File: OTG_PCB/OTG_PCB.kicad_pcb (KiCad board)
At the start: 2 copper layers, 44.9 x 35 mm, 14 parts, among them J1 USB_C_Receptacle_USB2.0, J2 USB_MINI_B, J3 USB_A, J4 USB_MINI_B, J5 USB_C_Receptacle_USB2.0, U1 USB3740B-AI2, U2 TUSB320IRWBR

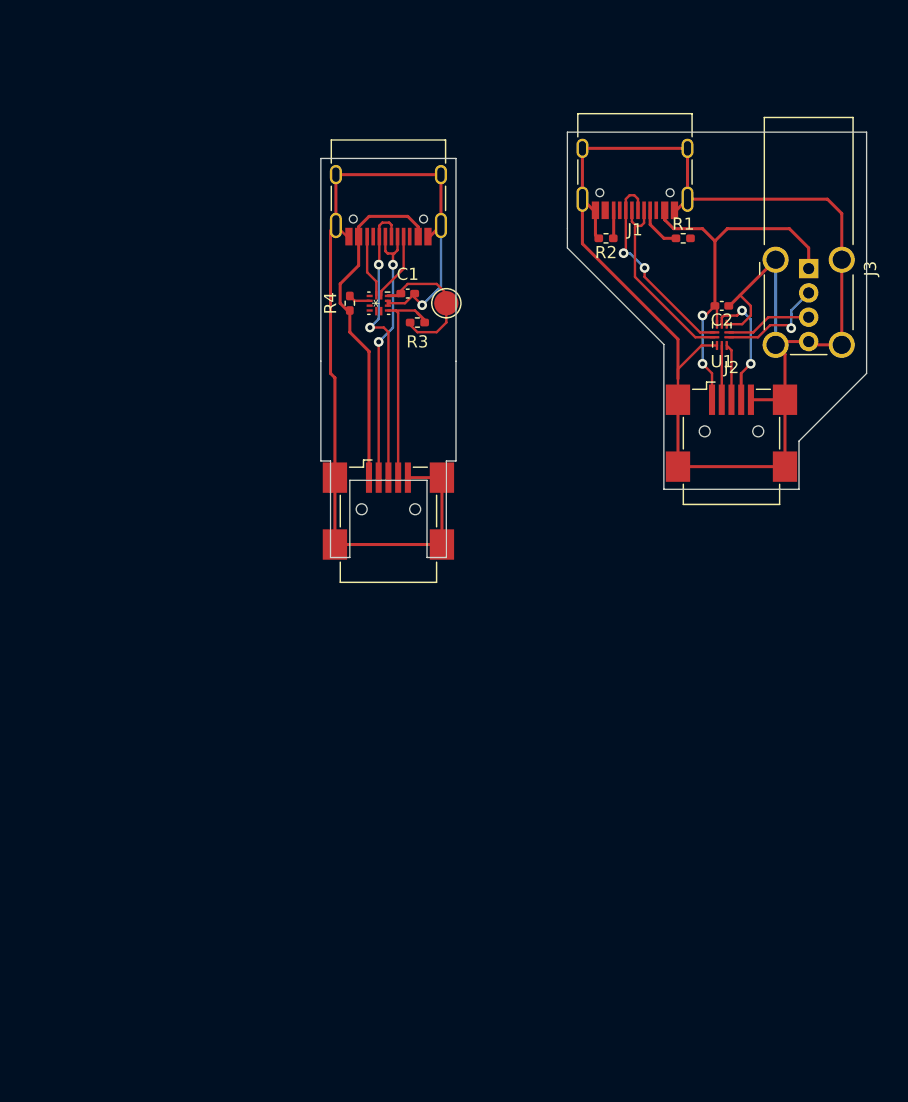
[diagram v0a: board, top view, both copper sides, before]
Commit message: Single layer, flex only
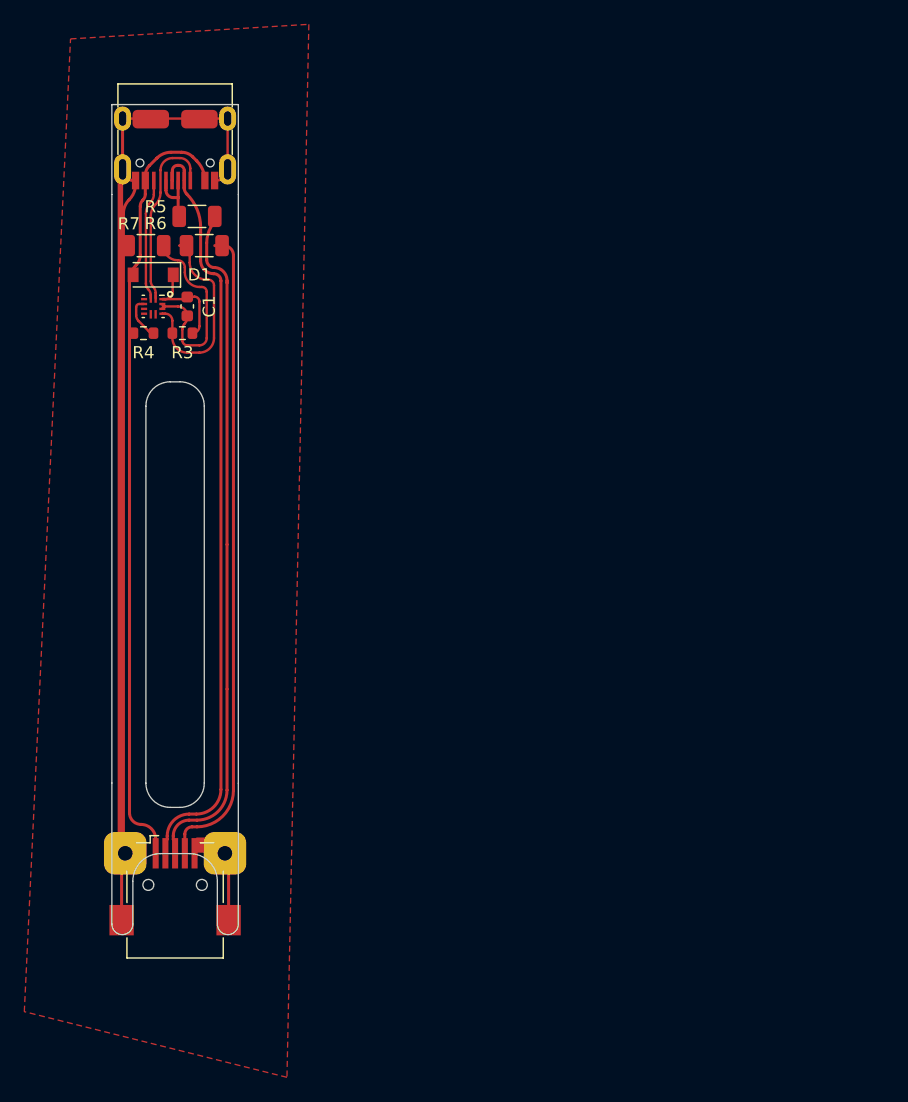
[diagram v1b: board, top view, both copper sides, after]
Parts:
- removed C2: 100n, Capacitor_SMD:C_0402_1005Metric_Pad0.74x0.62mm_HandSolder
- removed J1: USB_C_Receptacle_USB2.0, Connector_USB:USB_C_Receptacle_HRO_TYPE-C-31-M-12
- removed J2: USB_MINI_B, Connector_USB:USB_Mini-B_Wuerth_65100516121_Horizontal
- removed J3: USB_A, Connector_USB:USB_A_Wuerth_614004134726_Horizontal
- removed R1, R2: 5.1k, Resistor_SMD:R_0402_1005Metric_Pad0.72x0.64mm_HandSolder
- removed TP1: TestPoint, TestPoint:TestPoint_Pad_D2.0mm
- removed U1: USB3740B-AI2, Package_DFN_QFN:UQFN-10_1.3x1.8mm_P0.4mm
- added D1: D_Small, Diode_SMD:D_SOD-123, F.Cu at (109.2, 82.6)
- added R5: 0, Resistor_SMD:R_1206_3216Metric, F.Cu at (112.8, 77.8)
- added R6: 0, Resistor_SMD:R_1206_3216Metric, F.Cu at (113.4, 80.2)
- added R7: 0, Resistor_SMD:R_1206_3216Metric, F.Cu at (108.6, 80.2)
- C1: footprint Capacitor_SMD:C_0402_1005Metric_Pad0.74x0.62mm_HandSolder -> Capacitor_SMD:C_0603_1608Metric
- R3, R4: footprint Resistor_SMD:R_0402_1005Metric_Pad0.72x0.64mm_HandSolder -> Resistor_SMD:R_0603_1608Metric
- moved J4 35.5 mm to (111.0, 132.8)
- moved R3 19.3 mm to (111.6, 87.4), turned to 180 degrees
- moved U2 18.6 mm to (109.2, 85.2)
- moved C1 18.2 mm to (112.0, 85.2), turned to 90 degrees
- moved J5 18.1 mm to (111.0, 70.8)
- moved R4 17.1 mm to (108.4, 87.4), turned to 0 degrees
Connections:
- net VBUS renamed V+
- C1 pad 1: GND -> Net-(U2-Pad10)
- J4 pad : (no net) -> V-
- J4 pad 5: GND -> V-
- J4 pad 6: GND -> V-
- J5 pad : (no net) -> V-
- J5 pad A1: GND -> V-
- J5 pad A12: GND -> V-
- J5 pad A6: D+ -> Net-(J5-PadA6)
- J5 pad B1: GND -> V-
- J5 pad B12: GND -> V-
- J5 pad B6: D+ -> Net-(J5-PadA6)
- R3 pad 2: ID -> Net-(U2-Pad9)
- U2 pad 10: GND -> Net-(U2-Pad10)
- U2 pad 11: GND -> Net-(U2-Pad10)
- U2 pad 9: ID -> Net-(U2-Pad9)
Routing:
- net V-: track 0.00 -> 213.5 mm
- net GND: track 196.1 -> 0.00 mm, vias 1 -> 0
- net D-: track 22.5 -> 62.3 mm, vias 2 -> 0
- net ID: track 17.4 -> 53.4 mm
- net D+: track 24.5 -> 56.4 mm, vias 2 -> 0
- net Net-(J1-PadA6): track 17.3 -> 0.00 mm, vias 2 -> 0
- net Net-(U2-Pad10): track 0.00 -> 17.1 mm
- net Net-(U2-Pad9): track 0.00 -> 16.5 mm
- net Net-(J1-PadA7): track 16.1 -> 0.00 mm
- net SEL: track 10.4 -> 0.00 mm, vias 2 -> 0
- net CC1: track 5.59 -> 15.3 mm
- net Net-(J3-Pad2): track 9.42 -> 0.00 mm, vias 1 -> 0
- net Net-(J3-Pad3): track 7.06 -> 0.00 mm
- net Net-(J5-PadA6): track 0.00 -> 5.29 mm
- net V+: track 60.4 -> 65.3 mm, vias 2 -> 0
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- added copper zone on F.Cu, net V-
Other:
- board size 44.9 x 35 mm -> 10.4 x 68.3 mm
